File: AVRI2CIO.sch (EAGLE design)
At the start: 39 parts, among them IC1 MEGA8-P

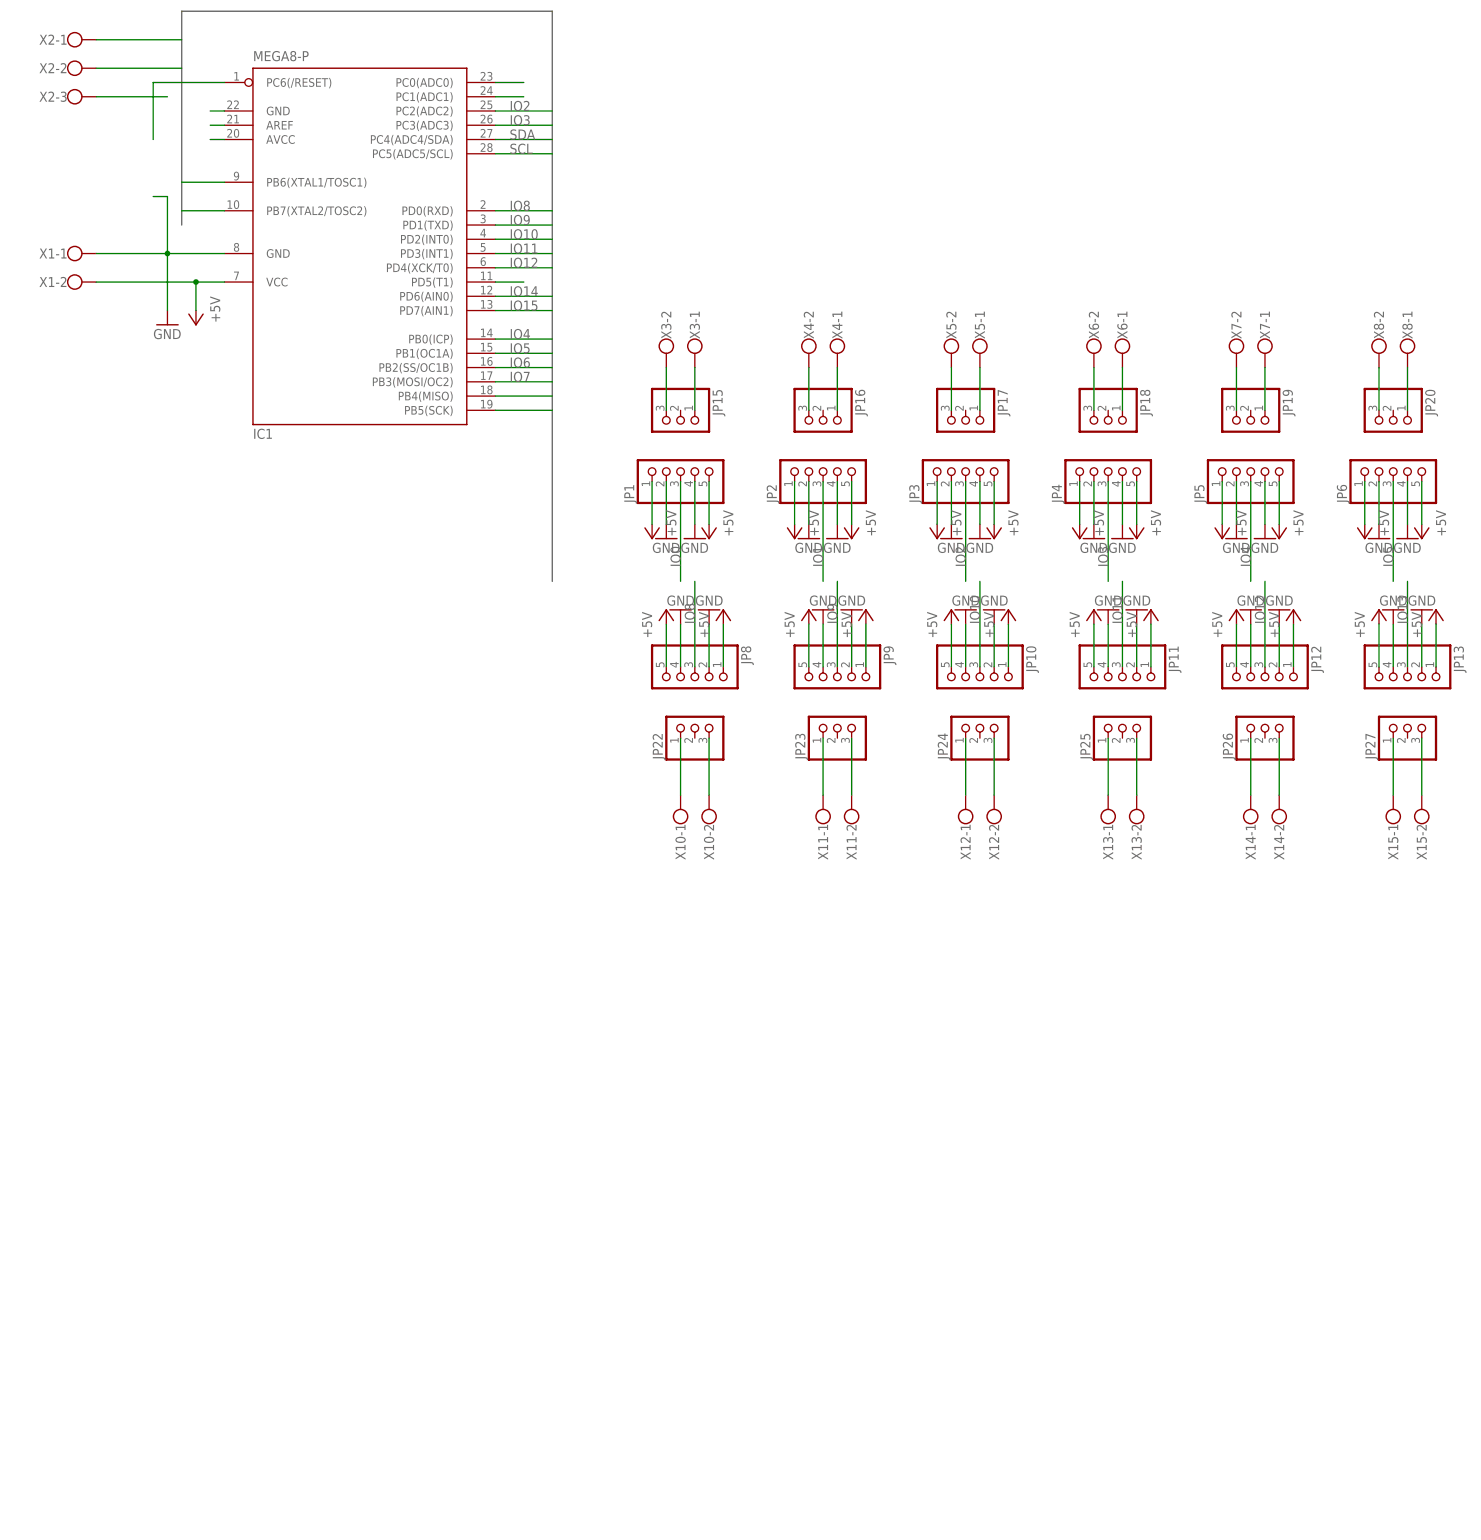
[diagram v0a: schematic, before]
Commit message: Schema  rename some items Board   move some items -> now 12 IO + I2C + Power connectors
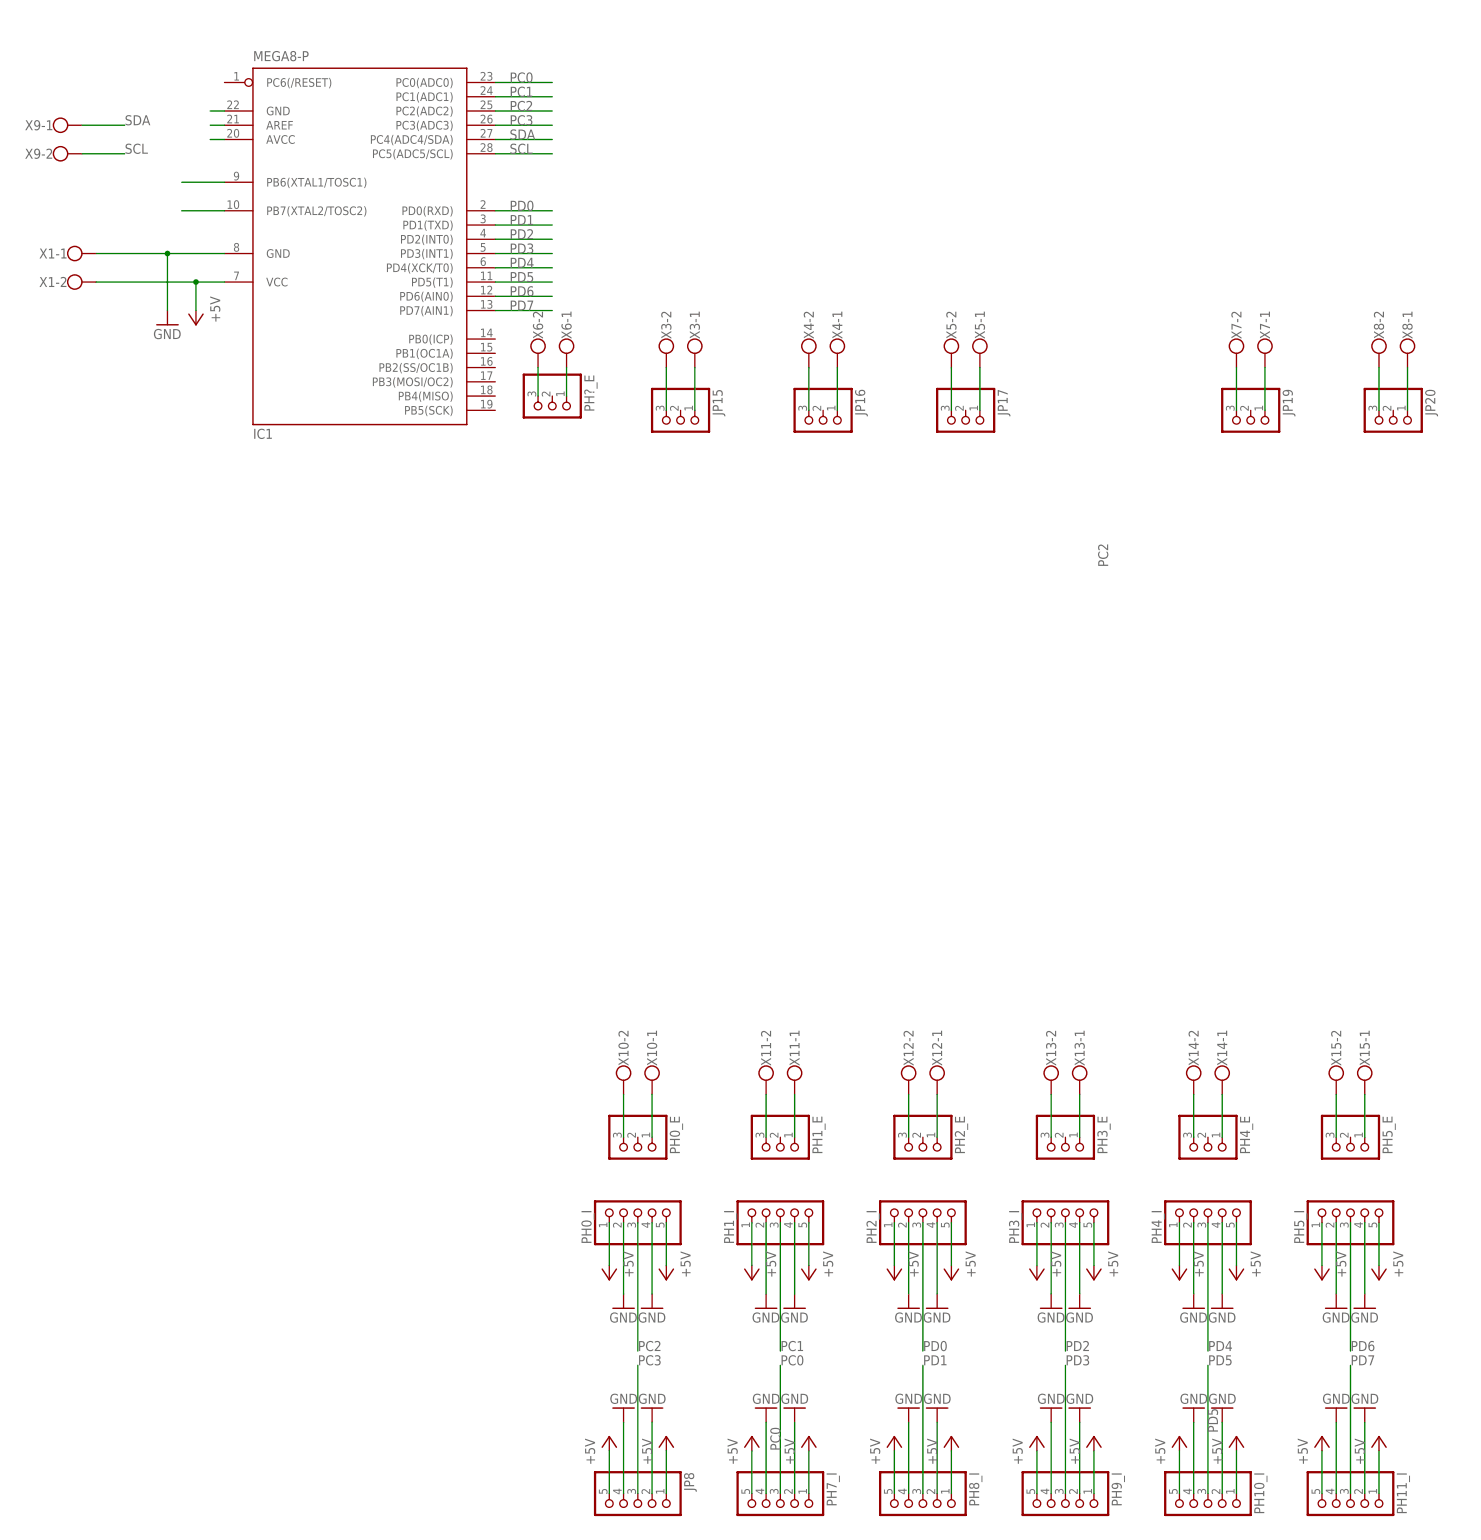
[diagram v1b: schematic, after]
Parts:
- removed JP1, JP10, JP11, JP12, JP13, JP2, JP3, JP4, JP5, JP6, JP9: (no value), pinhead:PINHD-1X5
- removed JP18, JP22, JP23, JP24, JP25, JP26, JP27: (no value), pinhead:PINHD-1X3
- removed X2: (no value), con-wago-500:W237-103
- added PH0_E, PH1_E, PH2_E, PH3_E, PH4_E, PH5_E, PH?_E: (no value), pinhead:PINHD-1X3
- added PH0_I, PH10_I, PH11_I, PH1_I, PH2_I, PH3_I, PH4_I, PH5_I, PH7_I, PH8_I, PH9_I: (no value), pinhead:PINHD-1X5
- added X9: (no value), con-wago-500:W237-102
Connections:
- removed net IO0: IC1.PD5(T1), JP1.3
- removed net IO10: IC1.PD2(INT0), JP10.3
- removed net IO11: IC1.PD3(INT1), JP11.3
- removed net IO12: IC1.PD4(XCK/T0), JP12.3
- removed net IO14: IC1.PD6(AIN0)
- removed net IO15: IC1.PD7(AIN1)
- removed net IO2: IC1.PC2(ADC2), JP3.3
- removed net IO3: IC1.PC3(ADC3), JP4.3
- removed net IO4: IC1.PB0(ICP), JP5.3
- removed net IO5: IC1.PB1(OC1A), JP6.3
- removed net IO6: IC1.PB2(SS/OC1B)
- removed net IO7: IC1.PB3(MOSI/OC2)
- removed net IO8: IC1.PD0(RXD), JP8.3
- removed net IO9: IC1.PD1(TXD), JP9.3
- removed net N$18: JP22.3, X10-2.KL
- removed net N$2: IC1.PC6(/RESET)
- removed net N$21: IC1.PB4(MISO)
- removed net N$22: IC1.PB5(SCK)
- removed net N$32: IC1.PC0(ADC0)
- new net PC0: IC1.PC0(ADC0), PH7_I.3
- new net PC1: IC1.PC1(ADC1), PH1_I.3
- new net PC2: IC1.PC2(ADC2), PH0_I.3
- new net PC3: IC1.PC3(ADC3), JP8.3
- new net PD0: IC1.PD0(RXD), PH2_I.3
- new net PD1: IC1.PD1(TXD), PH8_I.3
- new net PD2: IC1.PD2(INT0), PH3_I.3
- new net PD3: IC1.PD3(INT1), PH9_I.3
- new net PD4: IC1.PD4(XCK/T0), PH4_I.3
- new net PD5: IC1.PD5(T1), PH10_I.3
- new net PD6: IC1.PD6(AIN0), PH5_I.3
- new net PD7: IC1.PD7(AIN1), PH11_I.3
- net +5V: now also PH0_I.1, PH0_I.5, PH10_I.1, PH10_I.5, PH11_I.1, PH11_I.5, PH1_I.1, PH1_I.5, PH2_I.1, PH2_I.5, PH3_I.1, PH3_I.5, PH4_I.1, PH4_I.5, PH5_I.1, PH5_I.5, PH7_I.1, PH7_I.5, PH8_I.1, PH8_I.5, PH9_I.1, PH9_I.5; no longer JP1.1, JP1.5, JP10.1, JP10.5, JP11.1, JP11.5, JP12.1, JP12.5, JP13.1, JP13.5, JP2.1, JP2.5, JP3.1, JP3.5, JP4.1, JP4.5, JP5.1, JP5.5, JP6.1, JP6.5, JP9.1, JP9.5
- net GND: now also PH0_I.2, PH0_I.4, PH10_I.2, PH10_I.4, PH11_I.2, PH11_I.4, PH1_I.2, PH1_I.4, PH2_I.2, PH2_I.4, PH3_I.2, PH3_I.4, PH4_I.2, PH4_I.4, PH5_I.2, PH5_I.4, PH7_I.2, PH7_I.4, PH8_I.2, PH8_I.4, PH9_I.2, PH9_I.4; no longer JP1.2, JP1.4, JP10.2, JP10.4, JP11.2, JP11.4, JP12.2, JP12.4, JP13.2, JP13.4, JP2.2, JP2.4, JP3.2, JP3.4, JP4.2, JP4.4, JP5.2, JP5.4, JP6.2, JP6.4, JP9.2, JP9.4, X2-1.KL
- net IO1: no longer JP2.3
- net IO13: no longer JP13.3
- net N$1: now also PH0_E.3, X10-2.KL; no longer IC1.PC1(ADC1)
- net N$10: now also PH?_E.1; no longer JP18.1
- net N$17: now also PH0_E.1; no longer JP22.1
- net N$19: now also PH1_E.1; no longer JP23.1
- net N$20: now also PH1_E.3; no longer JP23.3
- net N$23: now also PH2_E.1; no longer JP24.1
- net N$24: now also PH2_E.3; no longer JP24.3
- net N$25: now also PH3_E.1; no longer JP25.1
- net N$26: now also PH3_E.3; no longer JP25.3
- net N$27: now also PH4_E.1; no longer JP26.1
- net N$28: now also PH4_E.3; no longer JP26.3
- net N$29: now also PH5_E.1; no longer JP27.1
- net N$30: now also PH5_E.3; no longer JP27.3
- net N$9: now also PH?_E.3; no longer JP18.3
- net SCL: now also X9-2.KL; no longer X2-2.KL
- net SDA: now also X9-1.KL; no longer X2-3.KL
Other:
- moved on the sheet: JP8, X10-1, X10-2, X11-1, X11-2, X12-1, X12-2, X13-1, X13-2, X14-1, X14-2, X15-1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
